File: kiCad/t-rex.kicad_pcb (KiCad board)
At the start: 2 copper layers, 230.2 x 96.8 mm, 123 parts, among them J0 Conn_01x03, SW0 MX, SW1 MX, SW10 MX, SW11 MX, SW12 MX, SW13 MX, SW14 MX, SW15 MX, SW16 MX, SW17 MX, SW18 MX, SW19 MX, SW2 MX, SW20 MX, SW21 MX, SW22 MX, SW23 MX, SW24 MX, SW25 MX, SW26 MX, SW27 MX, SW28 MX, SW29 MX, SW3 MX, SW30 MX, SW31 MX, SW32 MX, SW33 MX, SW34 MX, SW35 MX, SW36 MX, SW37 MX, SW38 MX, SW39 MX, SW4 MX, SW40 MX, SW41 MX, SW42 MX, SW43 MX, SW44 MX, SW45 MX, SW46 MX, SW47 MX, SW48 MX, SW49 MX, SW5 MX, SW50 MX, SW51 MX, SW52 MX, SW53 MX, SW54 MX, SW55 MX, SW56 MX, SW57 MX, SW58 MX, SW59 MX, SW6 MX, SW61 MX, SW7 MX, SW8 MX, SW9 MX, U0 Sparkfun_Pro_Micro

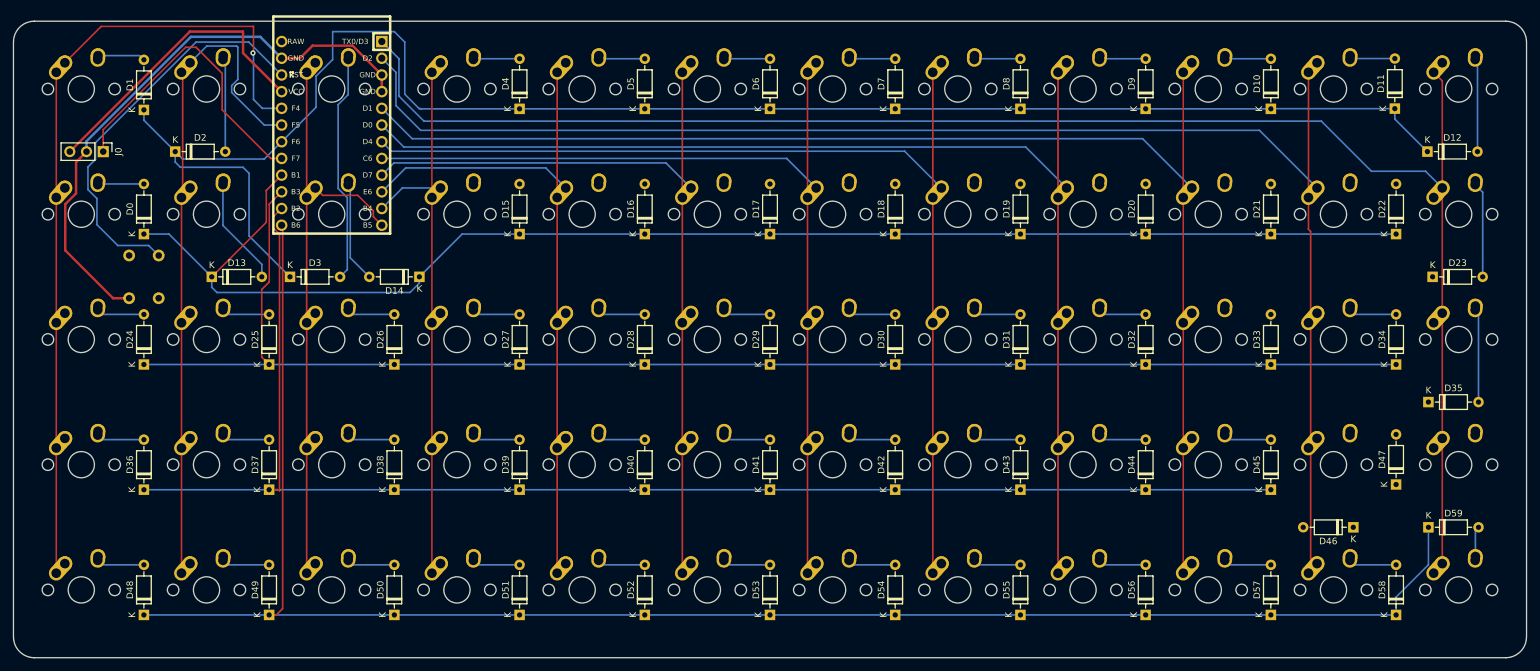
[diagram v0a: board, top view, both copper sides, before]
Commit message: add gerbers, fix labels
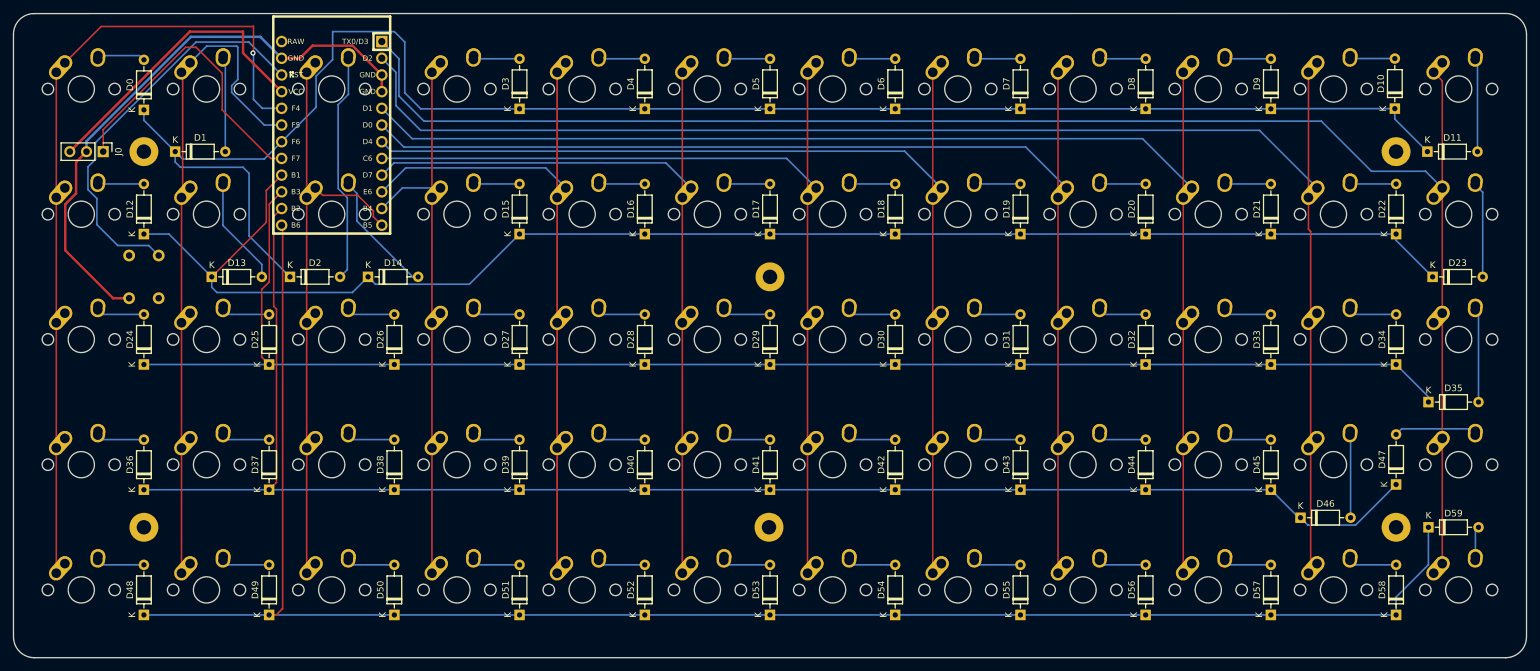
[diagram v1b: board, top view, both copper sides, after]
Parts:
- added ?: , , F.Cu at (242.9, 42.9)
- added ?: , , F.Cu at (52.4, 42.9)
- added ?: , , F.Cu at (147.6, 61.9)
- added ?: , , F.Cu at (52.4, 100.0)
- added ?: , , F.Cu at (242.9, 100.0)
- added ?: , , F.Cu at (147.5, 100.0)
- moved D46 8.16 mm to (228.3, 98.6), turned to 0 degrees
- moved D14 7.81 mm to (86.5, 61.9), turned to 0 degrees
- renumbered D1 to D0, D2 to D1, D11 to D10, D12 to D11, D0 to D12, D3 to D2, D4 to D3, D5 to D4, D6 to D5, D7 to D6, D8 to D7, D9 to D8, D10 to D9, SW1 to SW0, SW2 to SW1, SW11 to SW10, SW12 to SW11, SW0 to SW12, SW3 to SW2, SW4 to SW3, SW5 to SW4, SW6 to SW5, SW7 to SW6, SW8 to SW7, SW9 to SW8, SW10 to SW9
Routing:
- net /ROW3: track 216.9 -> 239.2 mm
- net Net-(D47-Pad2): track 0.00 -> 12.8 mm
- net Net-(D46-Pad2): track 0.00 -> 12.6 mm
- net /ROW1: track 219.2 -> 228.4 mm
- net /ROW2: track 218.5 -> 226.2 mm
- net Net-(D33-Pad2): track 0.00 -> 7.31 mm
- net Net-(D21-Pad2): track 0.00 -> 7.07 mm
- net Net-(D19-Pad2): track 0.00 -> 7.07 mm
- net Net-(D16-Pad2): track 0.00 -> 7.07 mm
- net Net-(D20-Pad2): track 0.00 -> 7.07 mm
- net Net-(D18-Pad2): track 0.00 -> 7.07 mm
- net Net-(D15-Pad2): track 0.00 -> 7.07 mm
- net Net-(D22-Pad2): track 0.00 -> 7.07 mm
- net Net-(D17-Pad2): track 0.00 -> 7.07 mm
- net Net-(D14-Pad2): track 15.4 -> 18.9 mm
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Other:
- board size 230.2 x 96.8 mm -> 230.2 x 98 mm
